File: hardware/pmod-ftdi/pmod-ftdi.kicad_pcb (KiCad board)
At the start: 2 copper layers, 21.3 x 15.7 mm, 17 parts, among them J1 USB_B_Micro, J2 PMOD-1x6-MALE, U1 FT230XS-R

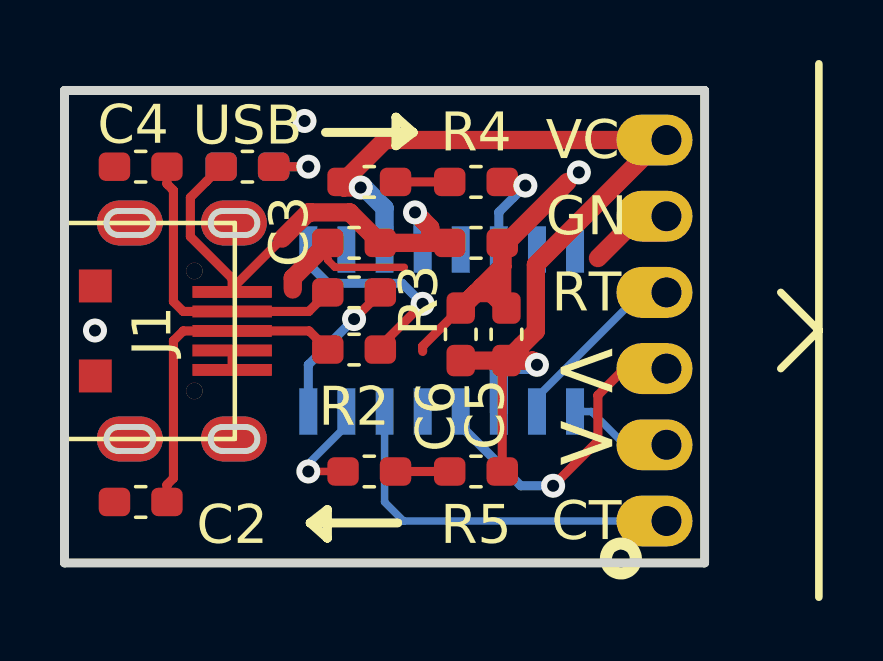
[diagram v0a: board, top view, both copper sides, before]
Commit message: pmod-ftdi: rev 1.1 - fix ft230xs package
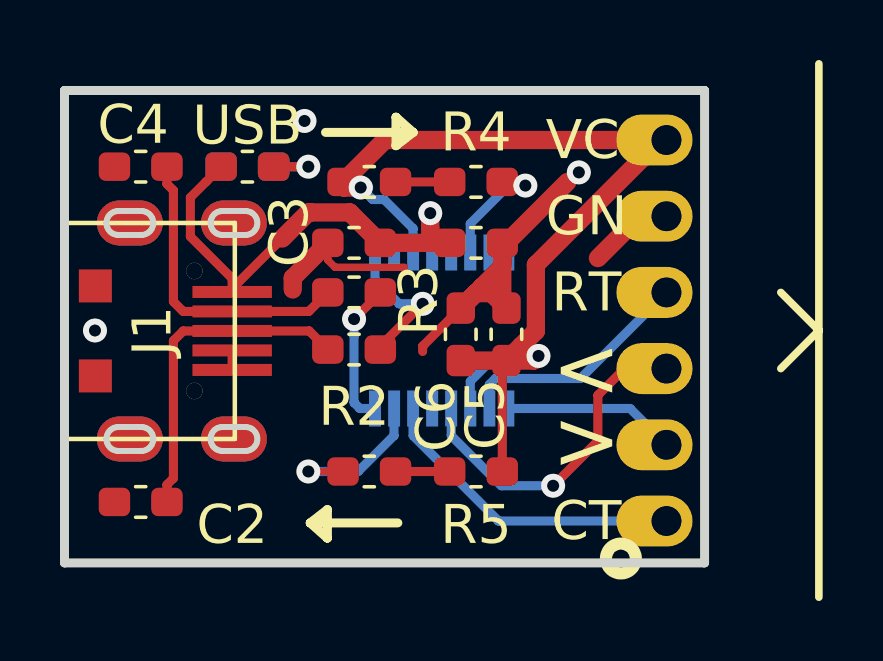
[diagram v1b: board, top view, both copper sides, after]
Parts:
- U1: footprint digikey-footprints:SOIC-16_W3.90mm -> tom-semiconductors:SSOP-16_3.9x4.9mm_P0.635mm
- turned U1 to 90 degrees
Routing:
- net /TXD: track 3.51 -> 7.16 mm
- net /RTS: track 6.24 -> 8.80 mm
- net /CTS: track 12.7 -> 10.5 mm
- net /D_P: track 6.95 -> 4.93 mm
- net /CBUS2: track 3.68 -> 5.67 mm
- net VCCIO: track 33.5 -> 35.2 mm
- net /CBUS1: track 3.32 -> 4.14 mm
- net /RXD: track 10.7 -> 11.3 mm
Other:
- board text added: "o"
- board text added: "tom@tomk.in v1.1"
- board text removed: "tom@tomk.in v1.0"

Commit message: pmod-ftdi : as built
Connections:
- U1 pad 8: /D_N -> /D_P
- U1 pad 9: /D_P -> /D_N
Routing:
- net /D_P: track 4.93 -> 6.26 mm
- net /D_N: track 4.82 -> 3.76 mm
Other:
- board text added: "tom@tomk.in v1.2"
- board text removed: "tom@tomk.in v1.1"
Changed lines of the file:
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@@
     (thickness 1.6)
     (drawings 22)
-    (tracks 135)
+    (tracks 132)
     (zones 0)
     (modules 17)
@@
   )
   (setup
-    (last_trace_width 0.25)
+    (last_trace_width 0.3048)
     (user_trace_width 0.3048)
     (user_trace_width 0.6096)
@@
       (net 10 "Net-(U1-Pad10)"))
     (pad 9 smd rect (at 2.6 -2.2225 90) (size 1.2 0.4) (layers B.Cu B.Paste B.Mask)
+      (net 7 /D_N))
+    (pad 8 smd rect (at -2.6 -2.2225 90) (size 1.2 0.4) (layers B.Cu B.Paste B.Mask)
       (net 6 /D_P))
-    (pad 8 smd rect (at -2.6 -2.2225 90) (size 1.2 0.4) (layers B.Cu B.Paste B.Mask)
-      (net 7 /D_N))
     (pad 7 smd rect (at -2.6 -1.5875 90) (size 1.2 0.4) (layers B.Cu B.Paste B.Mask)
       (net 15 /CBUS2))
@@
     (effects (font (size 1.3 1.3) (thickness 0.2)) (justify mirror))
   )
-  (gr_text "tom@tomk.in v1.1" (at 105.2195 92.0115) (layer B.SilkS)
+  (gr_text "tom@tomk.in v1.2" (at 105.2195 92.0115) (layer B.SilkS)
     (effects (font (size 1.3 1.3) (thickness 0.2)) (justify mirror))
   )
@@
   (segment (start 106.539 86.36) (end 106.539 86.247) (width 0.3048) (layer F.Cu) (net 6))
   (segment (start 106.539 86.247) (end 107.95 84.836) (width 0.3048) (layer F.Cu) (net 6))
-  (segment (start 107.1687 84.836) (end 106.3625 84.0298) (width 0.3048) (layer B.Cu) (net 6))
-  (segment (start 106.3625 84.0298) (end 106.3625 83.125) (width 0.3048) (layer B.Cu) (net 6))
-  (segment (start 107.95 84.836) (end 107.1687 84.836) (width 0.3048) (layer B.Cu) (net 6))
+  (segment (start 106.3625 86.4235) (end 106.3625 88.325) (width 0.3048) (layer B.Cu) (net 6))
+  (segment (start 107.95 84.836) (end 106.3625 86.4235) (width 0.3048) (layer B.Cu) (net 6))
   (via (at 105.664 85.344) (size 0.8) (drill 0.4) (layers F.Cu B.Cu) (net 7))
   (segment (start 106.539 84.455) (end 106.539 84.469) (width 0.3048) (layer F.Cu) (net 7))
   (segment (start 106.539 84.469) (end 105.664 85.344) (width 0.3048) (layer F.Cu) (net 7))
-  (segment (start 105.664 85.909685) (end 105.664 85.344) (width 0.3048) (layer B.Cu) (net 7))
-  (segment (start 105.664 88.1313) (end 105.664 85.909685) (width 0.3048) (layer B.Cu) (net 7))
-  (segment (start 105.8577 88.325) (end 105.664 88.1313) (width 0.3048) (layer B.Cu) (net 7))
-  (segment (start 106.3625 88.325) (end 105.8577 88.325) (width 0.3048) (layer B.Cu) (net 7))
+  (segment (start 106.3625 84.6455) (end 105.664 85.344) (width 0.3048) (layer B.Cu) (net 7))
+  (segment (start 106.3625 83.125) (end 106.3625 84.6455) (width 0.3048) (layer B.Cu) (net 7))
   (via (at 104.14 80.264) (size 0.8) (drill 0.4) (layers F.Cu B.Cu) (net 11))
   (segment (start 102.983 80.264) (end 104.14 80.264) (width 0.3048) (layer F.Cu) (net 11))
